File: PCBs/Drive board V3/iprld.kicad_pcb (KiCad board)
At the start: 2 copper layers, 100 x 80.1 mm, 39 parts, among them IC4 ADS1115IDGSR, J2 Conn_01x04_Pin, U15 AMS1117-3.3, U9 TCA9548APWR

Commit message: arm, drive and power modifications
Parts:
- added H1: MountingHole, MountingHole:MountingHole_3.2mm_M3_Pad_TopBottom, F.Cu at (128.1, 31.3)
- added H2: MountingHole, MountingHole:MountingHole_3.2mm_M3_Pad_TopBottom, F.Cu at (128.1, 102.4)
- added H3: MountingHole, MountingHole:MountingHole_3.2mm_M3_Pad_TopBottom, F.Cu at (37.1, 102.4)
- added H4: MountingHole, MountingHole:MountingHole_3.2mm_M3_Pad_TopBottom, F.Cu at (37.1, 31.4)
- added R1: 0R, Resistor_SMD:R_0805_2012Metric, F.Cu at (83.8, 75.3)
- moved CONTROL_R2 25.2 mm to (99.1, 27.8)
- moved C26 25.1 mm to (102.2, 35.9)
- moved J2 25.1 mm to (127.4, 86.0)
- moved R30 25.1 mm to (69.4, 51.6)
- moved R32 25.1 mm to (70.4, 76.2)
- moved U15 25.1 mm to (102.0, 43.0)
- moved MRS_RF1 25.1 mm to (98.8, 103.3)
- moved R29 25.1 mm to (74.0, 81.9)
- moved 12V_IN2 25.1 mm to (51.6, 70.2)
- moved C22 25.1 mm to (66.0, 51.6)
- moved C25 25.1 mm to (62.2, 76.0)
- moved C28 25.1 mm to (59.0, 59.0)
- moved C29 25.1 mm to (70.6, 81.9)
- moved I_LEFT2 25.1 mm to (65.0, 82.4)
- moved I_RIGHT2 25.1 mm to (59.6, 51.9)
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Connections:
- CONTROL_L2 pad 6: GNDPWR -> GND
- CONTROL_R2 pad 6: GNDPWR -> GND
- U2 pad 1: unconnected-(U2-3.3V-Pad1) -> Net-(U2-3.3V)
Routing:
- net GND: track 47.8 -> 73.8 mm, vias 11 -> 23
- net /+FUSE_R: track 11.5 -> 0.00 mm
- net +5V: track 215.7 -> 204.4 mm, vias 3 -> 2
- net +3.3V: track 179.9 -> 190.6 mm, vias 2 -> 4
- net +12V: track 10.5 -> 0.00 mm
- net /+12V_L: track 5.49 -> 0.43 mm
- net Net-(U2-3.3V): track 0.00 -> 3.91 mm
- net GNDPWR: track 2.74 -> 0.00 mm, vias 2 -> 0
- net /EN_L: track 38.8 -> 41.4 mm
- net /PWM_L: track 40.7 -> 43.2 mm
- net /SCL: track 81.2 -> 78.8 mm
- net /IN2_R: track 33.9 -> 36.3 mm
- net /IN1_L: track 24.6 -> 27.0 mm
- net /+12V_R: track 2.26 -> 0.00 mm
- net /IN1_R: track 35.4 -> 37.6 mm
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- removed copper zone on F.Cu, net GND

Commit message: i2c breakout correction, fuck you Maciej
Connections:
- MRS_LB1 pad 1: +3.3V -> /SCL_LB
- MRS_LB1 pad 2: /SCL_LB -> /SDA_LB
- MRS_LB1 pad 3: /SDA_LB -> +3.3V
- MRS_LF1 pad 1: +3.3V -> /SCL_LF
- MRS_LF1 pad 2: /SCL_LF -> /SDA_LF
- MRS_LF1 pad 3: /SDA_LF -> +3.3V
- MRS_RB1 pad 1: +3.3V -> /SCL_RB
- MRS_RB1 pad 2: /SCL_RB -> /SDA_RB
- MRS_RB1 pad 3: /SDA_RB -> +3.3V
- MRS_RF1 pad 1: +3.3V -> /SCL_RF
- MRS_RF1 pad 2: /SCL_RF -> /SDA_RF
- MRS_RF1 pad 3: /SDA_RF -> +3.3V
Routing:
- net +3.3V: track 190.6 -> 188.9 mm
- net /SDA_RF: track 9.21 -> 10.6 mm
- net /SCL_RF: track 9.46 -> 10.8 mm
- net /SCL_LF: track 16.1 -> 14.9 mm
- net /SDA_LB: track 7.92 -> 7.40 mm
- net /SDA_RB: track 18.2 -> 18.7 mm
- net /SDA_LF: track 16.4 -> 15.9 mm
- net /SCL_RB: track 18.4 -> 18.9 mm

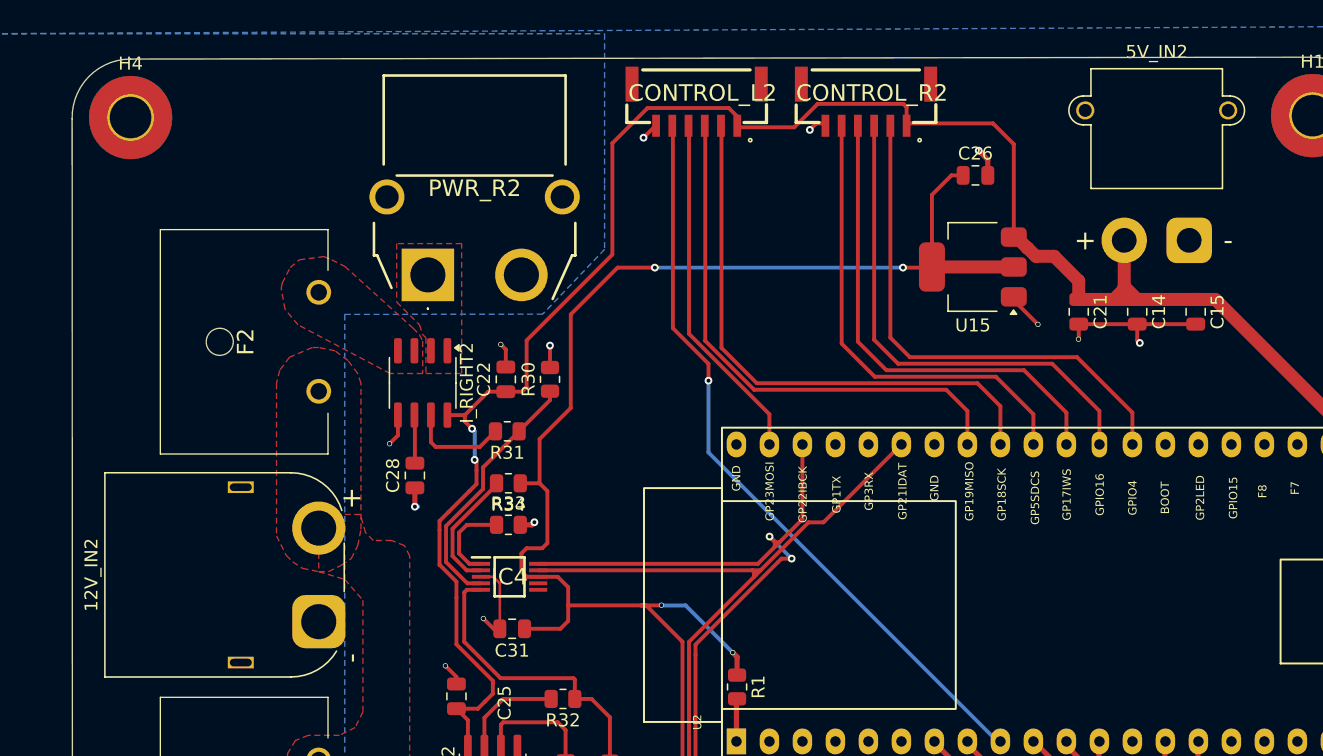
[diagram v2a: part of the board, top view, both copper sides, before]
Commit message: David half assed the motor reference change and didnt update the layout
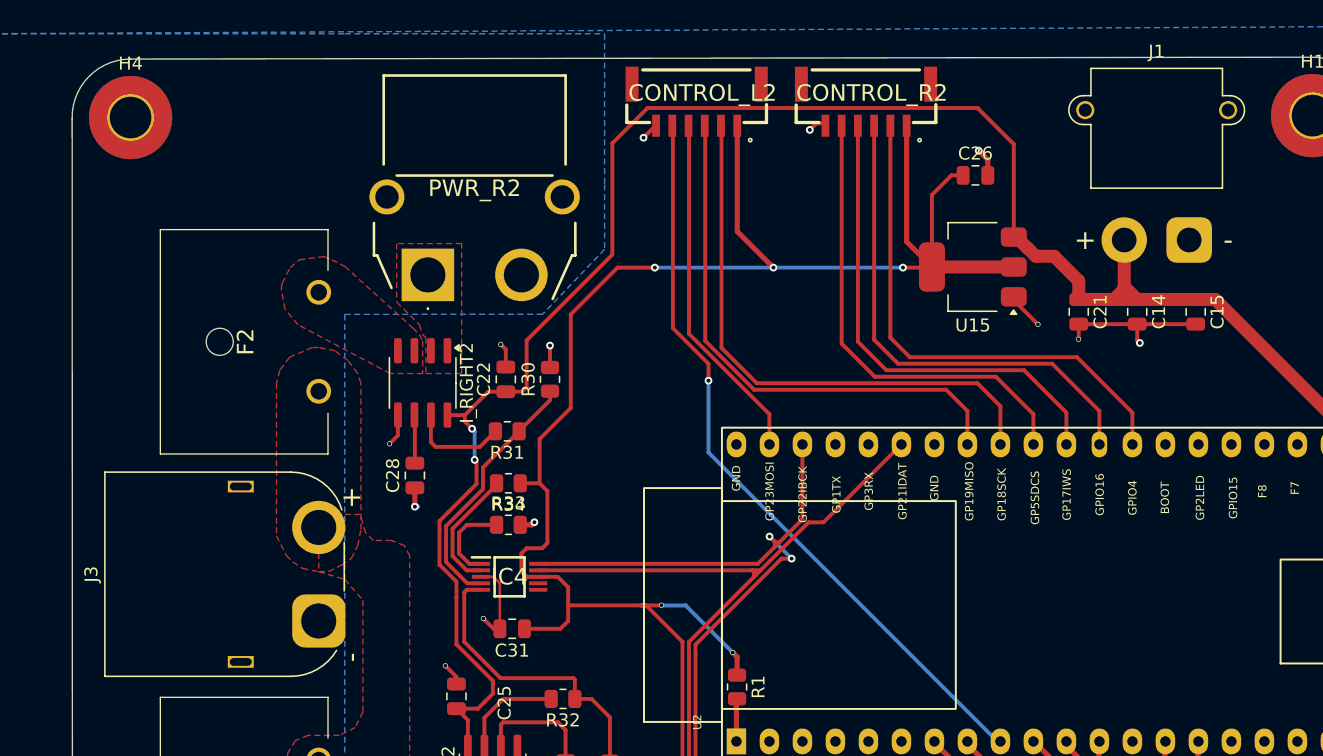
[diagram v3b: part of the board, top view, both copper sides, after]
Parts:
- removed 12V_IN2: XT60PW-F, Connector_AMASS:AMASS_XT60PW-M_1x02_P7.20mm_Horizontal
- removed 5V_IN2: XT30PW-F, Connector_AMASS:AMASS_XT30PW-M_1x02_P2.50mm_Horizontal
- added J1: Conn_01x02, Connector_AMASS:AMASS_XT30PW-M_1x02_P2.50mm_Horizontal, F.Cu at (118.6, 40.9)
- added J3: Conn_01x02, Connector_AMASS:AMASS_XT60PW-M_1x02_P7.20mm_Horizontal, F.Cu at (51.6, 70.2)
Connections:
- CONTROL_L2 pad 1: +5V -> +3.3V
- CONTROL_R2 pad 1: +5V -> +3.3V
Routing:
- net +3.3V: track 188.9 -> 213.8 mm, vias 4 -> 5
- net +5V: track 204.4 -> 201.4 mm

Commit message: drc clean boards
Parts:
- moved R29 1.84 mm to (74.0, 80.1)
- moved C29 1.76 mm to (70.6, 80.1)
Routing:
- net GND: track 73.8 -> 70.8 mm
- net /I_OUT_L: track 23.0 -> 21.2 mm
- net Net-(I_LEFT2-FILTER): track 9.40 -> 7.64 mm
- net +3.3V: track 213.8 -> 213.1 mm
